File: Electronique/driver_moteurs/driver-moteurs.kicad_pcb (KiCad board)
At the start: 2 copper layers, 51 parts, among them P1 CONN_ENCODER, P2 CONN_02_FREE, P3 CONN_I2C, P4 CONN_Servo, P5 CONN_FC, P6 CONN_SERIAL, P7 CONN_SWDIO, P8 CONN_CAN, U1 stm32f303k8t6, U10 Trou-3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

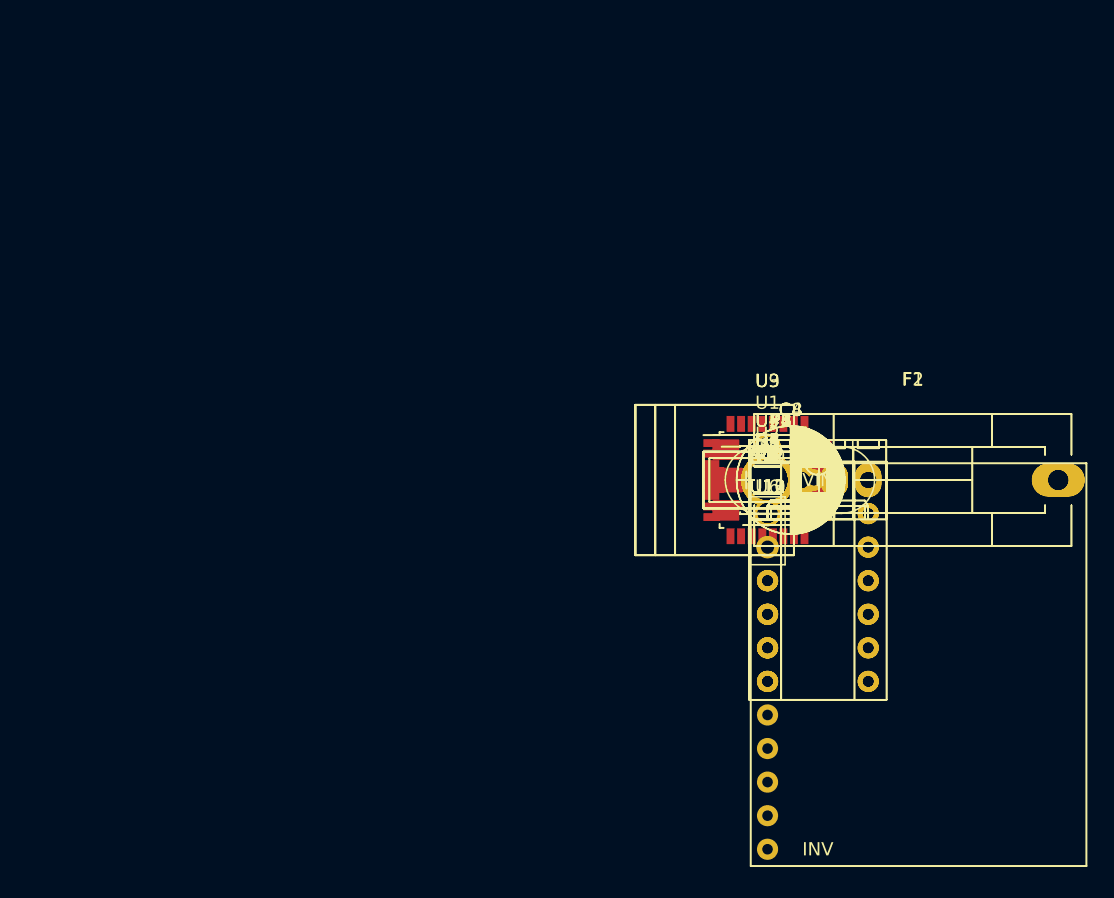
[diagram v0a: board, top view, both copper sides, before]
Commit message: Routage driver moteurs
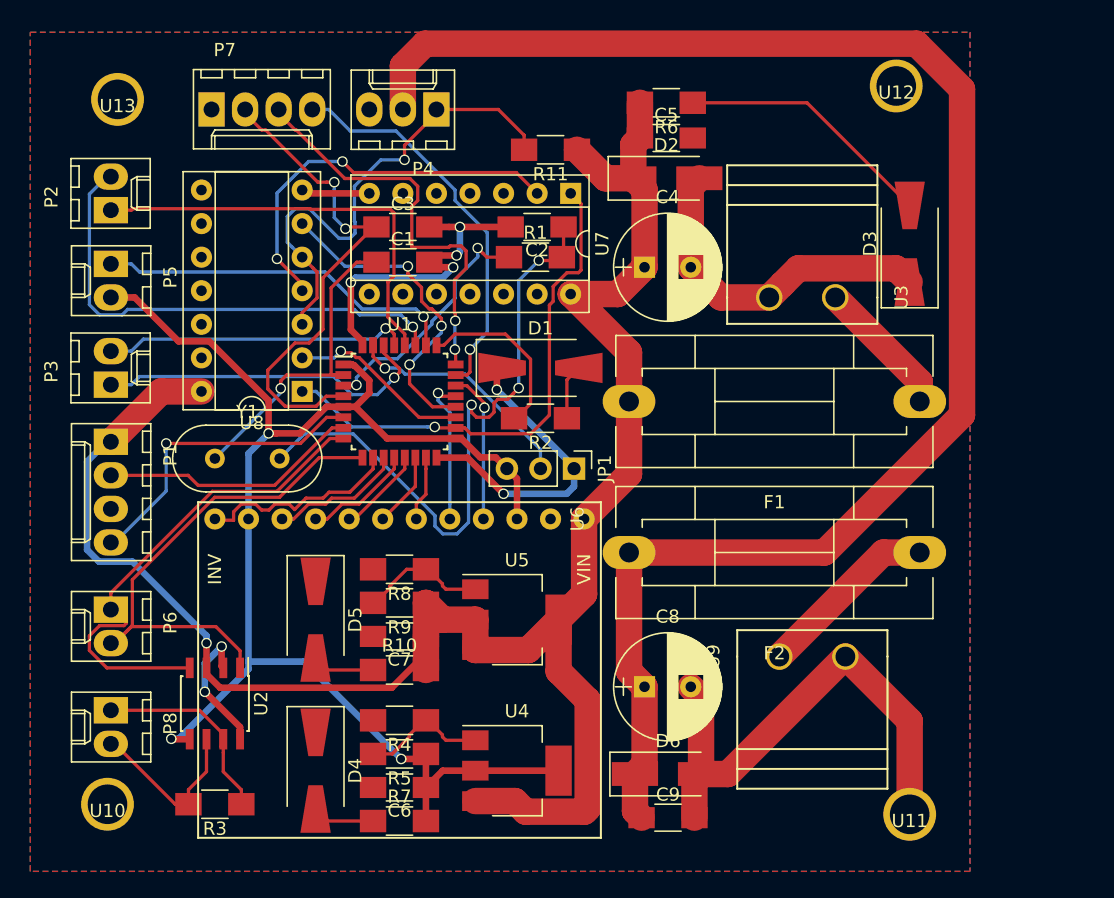
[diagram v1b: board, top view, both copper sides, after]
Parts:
- moved U13 57.0 mm to (99.3, 76.2)
- moved U10 55.7 mm to (98.6, 129.5)
- moved P2 53.7 mm to (98.8, 84.6), turned to 90 degrees
- moved P8 52.7 mm to (98.8, 122.4), turned to 270 degrees
- moved P5 52.3 mm to (98.8, 88.6), turned to 270 degrees
- moved P6 50.7 mm to (98.8, 114.8), turned to 270 degrees
- moved P7 50.6 mm to (106.4, 77.0)
- moved P3 50.2 mm to (98.8, 97.8), turned to 90 degrees
- moved P1 49.8 mm to (98.8, 102.1), turned to 270 degrees
- moved R3 48.5 mm to (106.7, 129.5), turned to 180 degrees
- moved U2 45.1 mm to (106.7, 121.9), turned to 270 degrees
- moved Y1 41.9 mm to (106.7, 103.4)
- moved D4 40.7 mm to (114.3, 127.0), turned to 270 degrees
- moved R7 38.0 mm to (120.7, 130.8)
- moved P4 37.6 mm to (123.4, 77.0), turned to 180 degrees
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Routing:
- net +5V: track 0.00 -> 147.9 mm, vias 0 -> 1
- net GND: track 0.00 -> 129.7 mm, vias 0 -> 8
- net +9V: track 0.00 -> 123.0 mm
- net +3V3: track 0.00 -> 107.7 mm, vias 0 -> 3
- net Net-(C2-Pad1): track 0.00 -> 48.1 mm, vias 0 -> 3
- net /EN_Servo: track 0.00 -> 39.2 mm, vias 0 -> 1
- net /RX: track 0.00 -> 38.9 mm
- net /nrst: track 0.00 -> 38.5 mm, vias 0 -> 2
- net /TX: track 0.00 -> 38.2 mm
- net Net-(P4-Pad1): track 0.00 -> 37.6 mm, vias 0 -> 1
- net Net-(P2-Pad2): track 0.00 -> 37.5 mm, vias 0 -> 1
- net Net-(P2-Pad1): track 0.00 -> 32.3 mm
- net /swclk: track 0.00 -> 31.2 mm, vias 0 -> 2
- net Net-(U7-Pad2): track 0.00 -> 29.8 mm, vias 0 -> 2
- net /swdio: track 0.00 -> 29.8 mm, vias 0 -> 1
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- added copper zone on B.Cu, net GND
- added copper zone on F.Cu, net GND
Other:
- net class Alim_3V added: clearance 0.2, trace_width 0.5, via_dia 0.8, via_drill 0.6
- net class Default: via_dia 0.6 -> 0.8; via_drill 0.4 -> 0.6
- net class alim added: clearance 0.2, trace_width 2, via_dia 0.8, via_drill 0.6

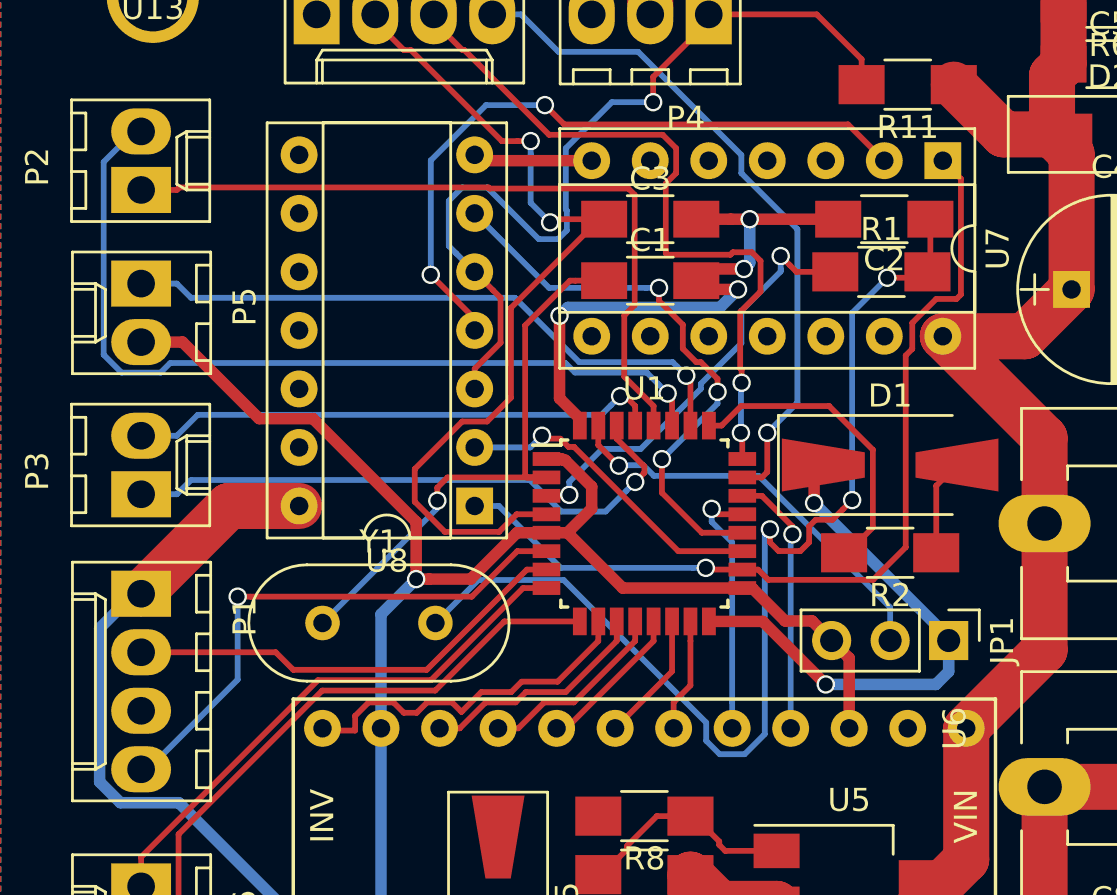
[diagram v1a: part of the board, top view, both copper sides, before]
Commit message: Correction B.Cu
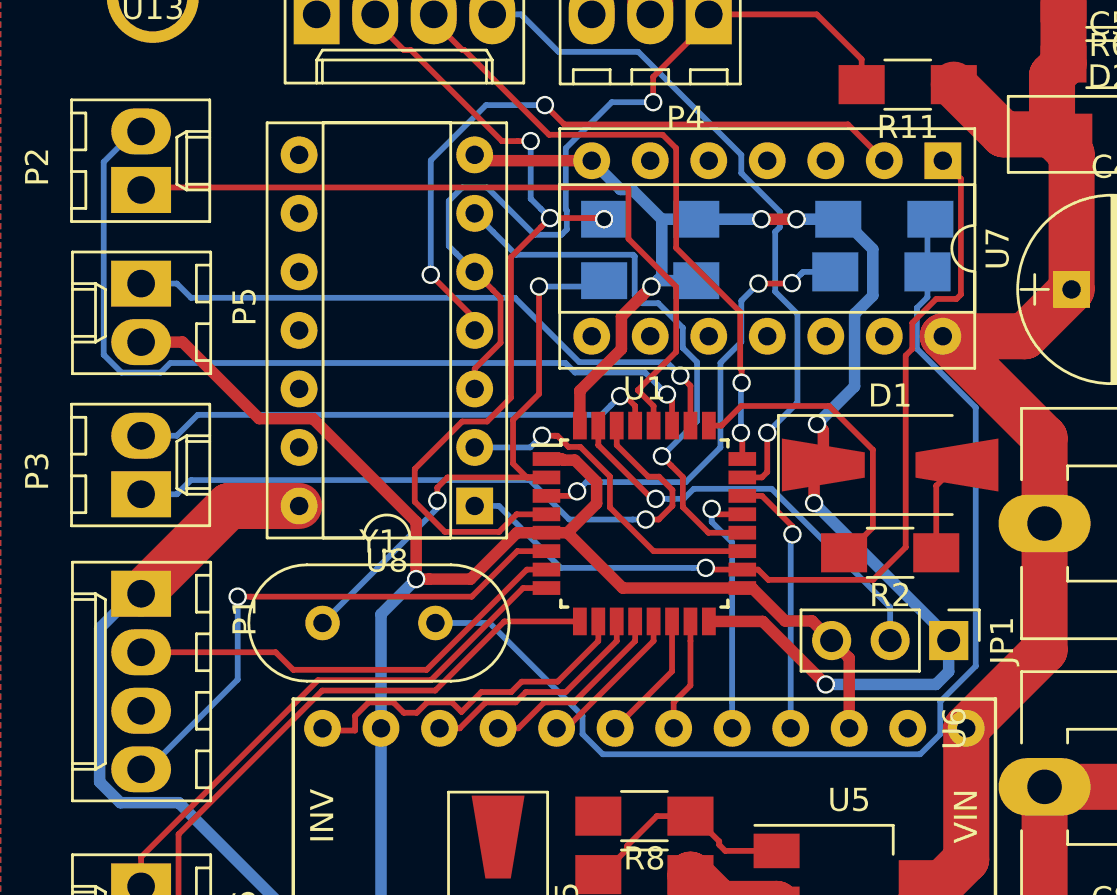
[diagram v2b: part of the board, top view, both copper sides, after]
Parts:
- C1, C2, C3, R1: moved to B.Cu
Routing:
- net GND: track 129.7 -> 140.7 mm
- net /swclk: track 31.2 -> 27.8 mm
- net /I2C_SCA: track 25.9 -> 29.0 mm
- net Net-(C2-Pad1): track 48.1 -> 49.4 mm, vias 3 -> 0
- net /nrst: track 38.5 -> 37.2 mm, vias 2 -> 3
- net Net-(C1-Pad1): track 24.6 -> 25.6 mm, vias 1 -> 2
- net Net-(P2-Pad1): track 32.3 -> 33.3 mm
- net Net-(R1-Pad1): track 18.8 -> 19.8 mm, vias 2 -> 3
- net /TX_Servo: track 13.9 -> 14.7 mm
- net /RX_Servo: track 24.6 -> 24.2 mm, vias 3 -> 1

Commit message: Putsch
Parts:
- U5: footprint TO_SOT_Packages_SMD:SOT-223-3Lead_TabPin2 -> TO_SOT_Packages_SMD:SOT-223-3_TabPin2
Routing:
- net +5V: track 147.9 -> 151.5 mm
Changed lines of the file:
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@@
     (uvia_drill 0.1)
     (add_net +3V3)
-    (add_net +5V)
     (add_net GND)
   )
@@
     (uvia_dia 0.3)
     (uvia_drill 0.1)
+    (add_net +5V)
     (add_net +9V)
     (add_net "Net-(F1-Pad1)")
@@
     )
   )
-  (module TO_SOT_Packages_SMD:SOT-223-3Lead_TabPin2 (layer F.Cu)
-    (at 129.54 115.57)
-    (descr "module CMS SOT223 4 pins")
-    (tags "CMS SOT")
-    (attr smd)
-    (fp_text reference U5 (at 0 -4.5) (layer F.SilkS)
-      (effects (font (size 1 1) (thickness 0.15)))
-    )
-    (fp_text value LM317_SOT223 (at 0 4.5) (layer F.Fab)
-      (effects (font (size 1 1) (thickness 0.15)))
-    )
-    (fp_text user %R (at 0 0 90) (layer F.Fab)
-      (effects (font (size 0.8 0.8) (thickness 0.12)))
-    )
-    (fp_line (start 1.91 3.41) (end 1.91 2.15) (layer F.SilkS) (width 0.12))
-    (fp_line (start 1.91 -3.41) (end 1.91 -2.15) (layer F.SilkS) (width 0.12))
-    (fp_line (start 4.4 -3.6) (end -4.4 -3.6) (layer F.CrtYd) (width 0.05))
-    (fp_line (start 4.4 3.6) (end 4.4 -3.6) (layer F.CrtYd) (width 0.05))
-    (fp_line (start -4.4 3.6) (end 4.4 3.6) (layer F.CrtYd) (width 0.05))
-    (fp_line (start -4.4 -3.6) (end -4.4 3.6) (layer F.CrtYd) (width 0.05))
-    (fp_line (start -1.85 -2.35) (end -0.85 -3.35) (layer F.Fab) (width 0.1))
-    (fp_line (start -1.85 -2.35) (end -1.85 3.35) (layer F.Fab) (width 0.1))
-    (fp_line (start -1.85 3.41) (end 1.91 3.41) (layer F.SilkS) (width 0.12))
-    (fp_line (start -0.85 -3.35) (end 1.85 -3.35) (layer F.Fab) (width 0.1))
-    (fp_line (start -4.1 -3.41) (end 1.91 -3.41) (layer F.SilkS) (width 0.12))
-    (fp_line (start -1.85 3.35) (end 1.85 3.35) (layer F.Fab) (width 0.1))
-    (fp_line (start 1.85 -3.35) (end 1.85 3.35) (layer F.Fab) (width 0.1))
-    (pad 2 smd rect (at 3.15 0) (size 2 3.8) (layers F.Cu F.Paste F.Mask)
-      (net 5 +5V))
-    (pad 2 smd rect (at -3.15 0) (size 2 1.5) (layers F.Cu F.Paste F.Mask)
-      (net 5 +5V))
-    (pad 3 smd rect (at -3.15 2.3) (size 2 1.5) (layers F.Cu F.Paste F.Mask)
-      (net 5 +5V))
-    (pad 1 smd rect (at -3.15 -2.3) (size 2 1.5) (layers F.Cu F.Paste F.Mask)
-      (net 32 "Net-(R8-Pad1)"))
-    (model ${KISYS3DMOD}/TO_SOT_Packages_SMD.3dshapes/SOT-223.wrl
-      (at (xyz 0 0 0))
-      (scale (xyz 1 1 1))
-      (rotate (xyz 0 0 0))
-    )
-  )
   (module Connectors_Molex:Molex_KK-6410-04_04x2.54mm_Straight (layer F.Cu)
     (at 106.426 76.962)
@@
     )
   )
+  (module TO_SOT_Packages_SMD:SOT-223-3_TabPin2 (layer F.Cu)
+    (at 129.54 115.57)
+    (descr "module CMS SOT223 4 pins")
+    (tags "CMS SOT")
+    (attr smd)
+    (fp_text reference U5 (at 0 -4.5) (layer F.SilkS)
+      (effects (font (size 1 1) (thickness 0.15)))
+    )
+    (fp_text value LM317_SOT223 (at 0 4.5) (layer F.Fab)
+      (effects (font (size 1 1) (thickness 0.15)))
+    )
+    (fp_text user %R (at 0 0 90) (layer F.Fab)
+      (effects (font (size 0.8 0.8) (thickness 0.12)))
+    )
+    (fp_line (start 1.91 3.41) (end 1.91 2.15) (layer F.SilkS) (width 0.12))
+    (fp_line (start 1.91 -3.41) (end 1.91 -2.15) (layer F.SilkS) (width 0.12))
+    (fp_line (start 4.4 -3.6) (end -4.4 -3.6) (layer F.CrtYd) (width 0.05))
+    (fp_line (start 4.4 3.6) (end 4.4 -3.6) (layer F.CrtYd) (width 0.05))
+    (fp_line (start -4.4 3.6) (end 4.4 3.6) (layer F.CrtYd) (width 0.05))
+    (fp_line (start -4.4 -3.6) (end -4.4 3.6) (layer F.CrtYd) (width 0.05))
+    (fp_line (start -1.85 -2.35) (end -0.85 -3.35) (layer F.Fab) (width 0.1))
+    (fp_line (start -1.85 -2.35) (end -1.85 3.35) (layer F.Fab) (width 0.1))
+    (fp_line (start -1.85 3.41) (end 1.91 3.41) (layer F.SilkS) (width 0.12))
+    (fp_line (start -0.85 -3.35) (end 1.85 -3.35) (layer F.Fab) (width 0.1))
+    (fp_line (start -4.1 -3.41) (end 1.91 -3.41) (layer F.SilkS) (width 0.12))
+    (fp_line (start -1.85 3.35) (end 1.85 3.35) (layer F.Fab) (width 0.1))
+    (fp_line (start 1.85 -3.35) (end 1.85 3.35) (layer F.Fab) (width 0.1))
+    (pad 2 smd rect (at 3.15 0) (size 2 3.8) (layers F.Cu F.Paste F.Mask)
+      (net 5 +5V))
+    (pad 2 smd rect (at -3.15 0) (size 2 1.5) (layers F.Cu F.Paste F.Mask)
+      (net 5 +5V))
+    (pad 3 smd rect (at -3.15 2.3) (size 2 1.5) (layers F.Cu F.Paste F.Mask)
+      (net 5 +5V))
+    (pad 1 smd rect (at -3.15 -2.3) (size 2 1.5) (layers F.Cu F.Paste F.Mask)
+      (net 32 "Net-(R8-Pad1)"))
+    (model ${KISYS3DMOD}/TO_SOT_Packages_SMD.3dshapes/SOT-223.wrl
+      (at (xyz 0 0 0))
+      (scale (xyz 1 1 1))
+      (rotate (xyz 0 0 0))
+    )
+  )
   (segment (start 116.078 88.773) (end 118.65 88.773) (width 0.25) (layer B.Cu) (net 1))
   (segment (start 118.65 88.773) (end 118.904 88.519) (width 0.25) (layer B.Cu) (net 1))
@@
   (segment (start 110.516 78.512) (end 114.46599 82.46199) (width 0.25) (layer F.Cu) (net 4))
   (segment (start 110.216 78.512) (end 110.516 78.512) (width 0.25) (layer F.Cu) (net 4))
-  (segment (start 132.69 115.57) (end 134.62 113.64) (width 2) (layer F.Cu) (net 5))
-  (segment (start 134.62 113.64) (end 134.62 107.95) (width 2) (layer F.Cu) (net 5))
-  (segment (start 126.39 129.3) (end 129.39 129.3) (width 2) (layer F.Cu) (net 5))
-  (segment (start 132.69 119.47) (end 132.69 115.57) (width 2) (layer F.Cu) (net 5))
-  (segment (start 134.890001 121.670001) (end 132.69 119.47) (width 2) (layer F.Cu) (net 5))
-  (segment (start 134.650001 130.100001) (end 134.890001 129.860001) (width 2) (layer F.Cu) (net 5))
-  (segment (start 134.890001 129.860001) (end 134.890001 121.670001) (width 2) (layer F.Cu) (net 5))
-  (segment (start 130.190001 130.100001) (end 134.650001 130.100001) (width 2) (layer F.Cu) (net 5))
-  (segment (start 129.39 129.3) (end 130.190001 130.100001) (width 2) (layer F.Cu) (net 5))
-  (segment (start 126.39 117.87) (end 130.39 117.87) (width 2) (layer F.Cu) (net 5))
-  (segment (start 130.39 117.87) (end 132.69 115.57) (width 2) (layer F.Cu) (net 5))
-  (segment (start 122.65 114.3) (end 123.92 115.57) (width 2) (layer F.Cu) (net 5))
-  (segment (start 123.92 115.57) (end 126.39 115.57) (width 2) (layer F.Cu) (net 5))
+  (segment (start 122.65 119.38) (end 130.130002 119.38) (width 2) (layer F.Cu) (net 5))
+  (segment (start 130.130002 119.38) (end 134.890001 124.139999) (width 2) (layer F.Cu) (net 5))
+  (segment (start 134.890001 124.139999) (end 134.890001 129.860001) (width 2) (layer F.Cu) (net 5))
+  (segment (start 134.890001 129.860001) (end 134.650001 130.100001) (width 2) (layer F.Cu) (net 5))
+  (segment (start 134.650001 130.100001) (end 130.729999 130.100001) (width 2) (layer F.Cu) (net 5))
+  (segment (start 130.729999 130.100001) (end 129.929998 129.3) (width 2) (layer F.Cu) (net 5))
+  (segment (start 129.929998 129.3) (end 129.39 129.3) (width 2) (layer F.Cu) (net 5))
+  (segment (start 129.39 129.3) (end 126.39 129.3) (width 2) (layer F.Cu) (net 5))
+  (segment (start 126.39 117.87) (end 123.68 117.87) (width 2) (layer F.Cu) (net 5))
+  (segment (start 123.68 117.87) (end 122.65 116.84) (width 2) (layer F.Cu) (net 5))
+  (segment (start 126.39 115.57) (end 126.39 117.87) (width 2) (layer F.Cu) (net 5))
+  (segment (start 132.69 115.57) (end 126.39 115.57) (width 2) (layer F.Cu) (net 5))
+  (segment (start 134.62 107.95) (end 134.62 113.64) (width 2) (layer F.Cu) (net 5))
+  (segment (start 134.62 113.64) (end 132.69 115.57) (width 2) (layer F.Cu) (net 5))
   (segment (start 122.65 116.84) (end 122.65 118.14) (width 0.5) (layer F.Cu) (net 5))
   (segment (start 122.65 118.14) (end 120.06999 120.72001) (width 0.5) (layer F.Cu) (net 5))
@@
   (segment (start 106.045 119.22) (end 106.045 117.348) (width 0.5) (layer F.Cu) (net 5))
   (via (at 106.045 117.348) (size 0.8) (drill 0.6) (layers F.Cu B.Cu) (net 5))
-  (segment (start 126.39 115.57) (end 126.39 117.87) (width 2) (layer F.Cu) (net 5))
   (segment (start 122.65 116.84) (end 122.65 114.3) (width 2) (layer F.Cu) (net 5))
   (segment (start 122.65 119.38) (end 122.65 116.84) (width 2) (layer F.Cu) (net 5))
@@
   (segment (start 122.5 123.19) (end 122.65 123.19) (width 0.25) (layer F.Cu) (net 31))
   (segment (start 126.39 113.27) (end 124.16 113.27) (width 0.25) (layer F.Cu) (net 32))
+  (segment (start 124.16 113.27) (end 123.9 113.01) (width 0.25) (layer F.Cu) (net 32))
   (segment (start 123.9 112.86) (end 122.8 111.76) (width 0.25) (layer F.Cu) (net 32))
+  (segment (start 122.8 111.76) (end 122.65 111.76) (width 0.25) (layer F.Cu) (net 32))
   (segment (start 123.9 113.01) (end 123.9 112.86) (width 0.25) (layer F.Cu) (net 32))
-  (segment (start 124.16 113.27) (end 123.9 113.01) (width 0.25) (layer F.Cu) (net 32))
   (segment (start 122.65 111.76) (end 121.19 111.76) (width 0.25) (layer F.Cu) (net 32))
   (segment (start 121.19 111.76) (end 119.9 113.05) (width 0.25) (layer F.Cu) (net 32))
@@
   (segment (start 119.9 113.2) (end 118.8 114.3) (width 0.25) (layer F.Cu) (net 32))
   (segment (start 118.8 114.3) (end 118.65 114.3) (width 0.25) (layer F.Cu) (net 32))
-  (segment (start 122.8 111.76) (end 122.65 111.76) (width 0.25) (layer F.Cu) (net 32))
   (segment (start 109.760001 106.824999) (end 108.679999 106.824999) (width 0.25) (layer F.Cu) (net 33))
   (segment (start 110.769988 107.27501) (end 110.210012 107.27501) (width 0.25) (layer F.Cu) (net 33))
